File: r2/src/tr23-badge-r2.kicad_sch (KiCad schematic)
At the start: 60 parts, among them Q1 MMBT3904-TP, Q2 MMBT3904-TP, Q3 MMBT3904-TP, Y1 32.768kHz

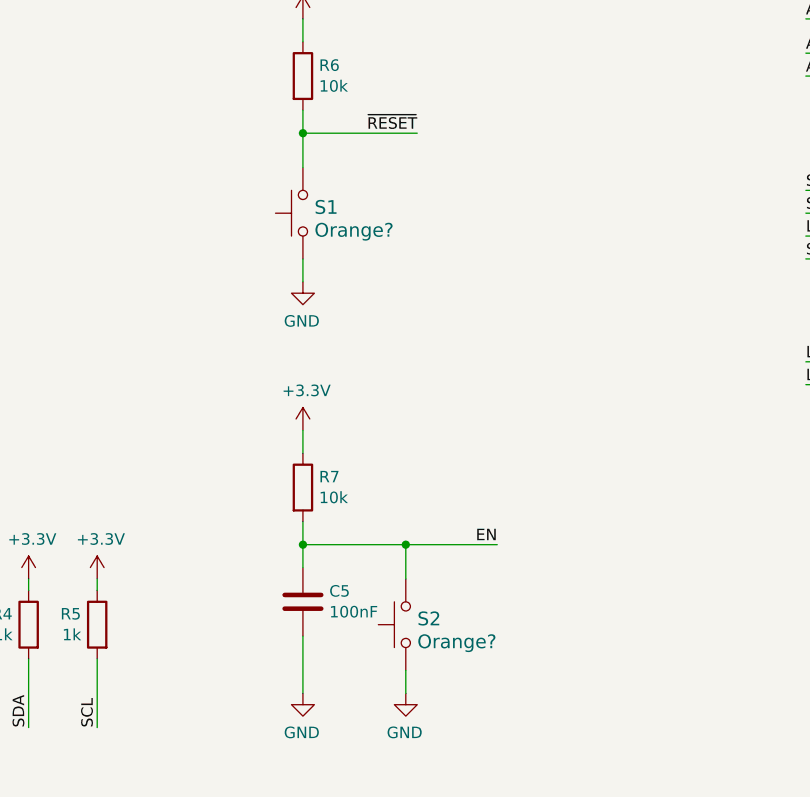
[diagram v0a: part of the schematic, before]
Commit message: Fix tactile switch symbols. By using a two-pin symbol rather than the truer 4-pin one, signals were shorted at the footprint
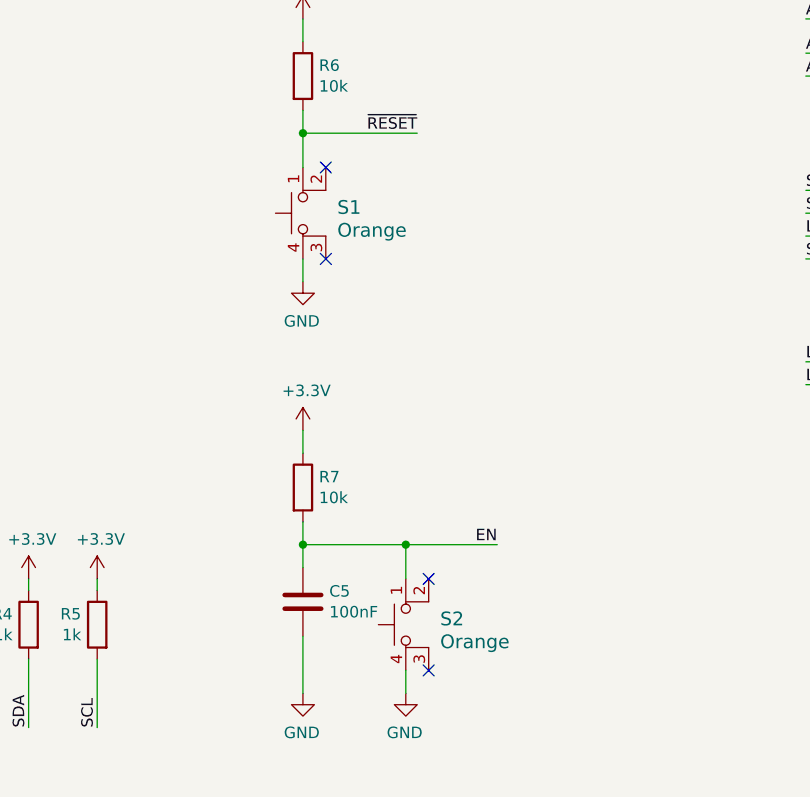
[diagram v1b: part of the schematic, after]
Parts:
- S1, S2: value Orange? -> Orange; symbol Switch:SW_Push -> Switch:SW_MEC_5E
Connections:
- net GND: now also S1.4 (A), S2.4 (A); no longer S1.2, S2.2
- no-connect marks 0 -> 4
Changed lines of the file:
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@@
   (junction (at 31.75 132.08) (diameter 0) (color 0 0 0 0)
   )
+  (no_connect (at 130.81 137.16))
+  (no_connect (at 142.24 172.72))
+  (no_connect (at 130.81 127))
+  (no_connect (at 142.24 182.88))
   (wire (pts (xy 195.58 129.54) (xy 184.15 129.54))
     (stroke (width 0) (type default))
@@
     )
   )
-  (symbol (lib_id "Switch:SW_Push") (at 128.27 132.08 90) (mirror x) (unit 1)
+  (symbol (lib_id "Switch:SW_MEC_5E") (at 130.81 132.08 90) (mirror x) (unit 1)
     (in_bom yes) (on_board yes) (dnp no) (fields_autoplaced)
-    (property "Reference" "S1" (at 129.54 131.445 90)
+    (property "Reference" "S1" (at 132.08 131.445 90)
       (effects (font (size 1.524 1.524)) (justify right))
     )
-    (property "Value" "Orange?" (at 129.54 133.985 90)
+    (property "Value" "Orange" (at 132.08 133.985 90)
       (effects (font (size 1.524 1.524)) (justify right))
     )
@@
       (effects (font (size 1.27 1.27)) hide)
     )
-    (property "Datasheet" "~" (at 123.19 132.08 0)
-      (effects (font (size 1.27 1.27)) hide)
-    )
-    (property "Digi-Key_PN" "CKN9112CT-ND" (at 118.11 137.16 0)
-      (effects (font (size 1.524 1.524)) (justify left) hide)
-    )
-    (property "MPN" "" (at 115.57 137.16 0)
-      (effects (font (size 1.524 1.524)) (justify left) hide)
-    )
-    (property "Category" "Switches" (at 113.03 137.16 0)
-      (effects (font (size 1.524 1.524)) (justify left) hide)
-    )
-    (property "Family" "Tactile Switches" (at 110.49 137.16 0)
-      (effects (font (size 1.524 1.524)) (justify left) hide)
-    )
-    (property "DK_Datasheet_Link" "https://www.ckswitches.com/media/1471/pts645.pdf" (at 107.95 137.16 0)
-      (effects (font (size 1.524 1.524)) (justify left) hide)
-    )
-    (property "DK_Detail_Page" "/product-detail/en/c-k/PTS645SM43SMTR92-LFS/CKN9112CT-ND/1146934" (at 105.41 137.16 0)
-      (effects (font (size 1.524 1.524)) (justify left) hide)
-    )
-    (property "Description" "SWITCH TACTILE SPST-NO 0.05A 12V" (at 102.87 137.16 0)
-      (effects (font (size 1.524 1.524)) (justify left) hide)
-    )
-    (property "Manufacturer" "C&K" (at 100.33 137.16 0)
-      (effects (font (size 1.524 1.524)) (justify left) hide)
-    )
-    (property "Status" "Active" (at 97.79 137.16 0)
+    (property "Datasheet" "http://www.apem.com/int/index.php?controller=attachment&id_attachment=1371" (at 123.19 132.08 0)
+      (effects (font (size 1.27 1.27)) hide)
+    )
+    (property "Digi-Key_PN" "CKN9112CT-ND" (at 120.65 137.16 0)
+      (effects (font (size 1.524 1.524)) (justify left) hide)
+    )
+    (property "MPN" "" (at 118.11 137.16 0)
+      (effects (font (size 1.524 1.524)) (justify left) hide)
+    )
+    (property "Category" "Switches" (at 115.57 137.16 0)
+      (effects (font (size 1.524 1.524)) (justify left) hide)
+    )
+    (property "Family" "Tactile Switches" (at 113.03 137.16 0)
+      (effects (font (size 1.524 1.524)) (justify left) hide)
+    )
+    (property "DK_Datasheet_Link" "https://www.ckswitches.com/media/1471/pts645.pdf" (at 110.49 137.16 0)
+      (effects (font (size 1.524 1.524)) (justify left) hide)
+    )
+    (property "DK_Detail_Page" "/product-detail/en/c-k/PTS645SM43SMTR92-LFS/CKN9112CT-ND/1146934" (at 107.95 137.16 0)
+      (effects (font (size 1.524 1.524)) (justify left) hide)
+    )
+    (property "Description" "SWITCH TACTILE SPST-NO 0.05A 12V" (at 105.41 137.16 0)
+      (effects (font (size 1.524 1.524)) (justify left) hide)
+    )
+    (property "Manufacturer" "C&K" (at 102.87 137.16 0)
+      (effects (font (size 1.524 1.524)) (justify left) hide)
+    )
+    (property "Status" "Active" (at 100.33 137.16 0)
       (effects (font (size 1.524 1.524)) (justify left) hide)
     )
     (pin "1")
     (pin "2")
+    (pin "3")
+    (pin "4")
     (instances
       (project "tr23-badge-r2"
@@
     )
   )
-  (symbol (lib_id "Switch:SW_Push") (at 139.7 177.8 90) (mirror x) (unit 1)
+  (symbol (lib_id "Switch:SW_MEC_5E") (at 142.24 177.8 90) (mirror x) (unit 1)
     (in_bom yes) (on_board yes) (dnp no) (fields_autoplaced)
-    (property "Reference" "S2" (at 140.97 177.165 90)
+    (property "Reference" "S2" (at 143.51 177.165 90)
       (effects (font (size 1.524 1.524)) (justify right))
     )
-    (property "Value" "Orange?" (at 140.97 179.705 90)
+    (property "Value" "Orange" (at 143.51 179.705 90)
       (effects (font (size 1.524 1.524)) (justify right))
     )
@@
       (effects (font (size 1.27 1.27)) hide)
     )
-    (property "Datasheet" "~" (at 134.62 177.8 0)
-      (effects (font (size 1.27 1.27)) hide)
-    )
-    (property "Digi-Key_PN" "CKN9112CT-ND" (at 129.54 182.88 0)
-      (effects (font (size 1.524 1.524)) (justify left) hide)
-    )
-    (property "MPN" "" (at 127 182.88 0)
-      (effects (font (size 1.524 1.524)) (justify left) hide)
-    )
-    (property "Category" "Switches" (at 124.46 182.88 0)
-      (effects (font (size 1.524 1.524)) (justify left) hide)
-    )
-    (property "Family" "Tactile Switches" (at 121.92 182.88 0)
-      (effects (font (size 1.524 1.524)) (justify left) hide)
-    )
-    (property "DK_Datasheet_Link" "https://www.ckswitches.com/media/1471/pts645.pdf" (at 119.38 182.88 0)
-      (effects (font (size 1.524 1.524)) (justify left) hide)
-    )
-    (property "DK_Detail_Page" "/product-detail/en/c-k/PTS645SM43SMTR92-LFS/CKN9112CT-ND/1146934" (at 116.84 182.88 0)
-      (effects (font (size 1.524 1.524)) (justify left) hide)
-    )
-    (property "Description" "SWITCH TACTILE SPST-NO 0.05A 12V" (at 114.3 182.88 0)
-      (effects (font (size 1.524 1.524)) (justify left) hide)
-    )
-    (property "Manufacturer" "C&K" (at 111.76 182.88 0)
-      (effects (font (size 1.524 1.524)) (justify left) hide)
-    )
-    (property "Status" "Active" (at 109.22 182.88 0)
+    (property "Datasheet" "http://www.apem.com/int/index.php?controller=attachment&id_attachment=1371" (at 134.62 177.8 0)
+      (effects (font (size 1.27 1.27)) hide)
+    )
+    (property "Digi-Key_PN" "CKN9112CT-ND" (at 132.08 182.88 0)
+      (effects (font (size 1.524 1.524)) (justify left) hide)
+    )
+    (property "MPN" "" (at 129.54 182.88 0)
+      (effects (font (size 1.524 1.524)) (justify left) hide)
+    )
+    (property "Category" "Switches" (at 127 182.88 0)
+      (effects (font (size 1.524 1.524)) (justify left) hide)
+    )
+    (property "Family" "Tactile Switches" (at 124.46 182.88 0)
+      (effects (font (size 1.524 1.524)) (justify left) hide)
+    )
+    (property "DK_Datasheet_Link" "https://www.ckswitches.com/media/1471/pts645.pdf" (at 121.92 182.88 0)
+      (effects (font (size 1.524 1.524)) (justify left) hide)
+    )
+    (property "DK_Detail_Page" "/product-detail/en/c-k/PTS645SM43SMTR92-LFS/CKN9112CT-ND/1146934" (at 119.38 182.88 0)
+      (effects (font (size 1.524 1.524)) (justify left) hide)
+    )
+    (property "Description" "SWITCH TACTILE SPST-NO 0.05A 12V" (at 116.84 182.88 0)
+      (effects (font (size 1.524 1.524)) (justify left) hide)
+    )
+    (property "Manufacturer" "C&K" (at 114.3 182.88 0)
+      (effects (font (size 1.524 1.524)) (justify left) hide)
+    )
+    (property "Status" "Active" (at 111.76 182.88 0)
       (effects (font (size 1.524 1.524)) (justify left) hide)
     )
     (pin "1")
     (pin "2")
-    (instances
-      (project "tr23-badge-r2"
+    (pin "3")
+    (pin "4")
+    (instances
+      (project "tr23-badge-r2"

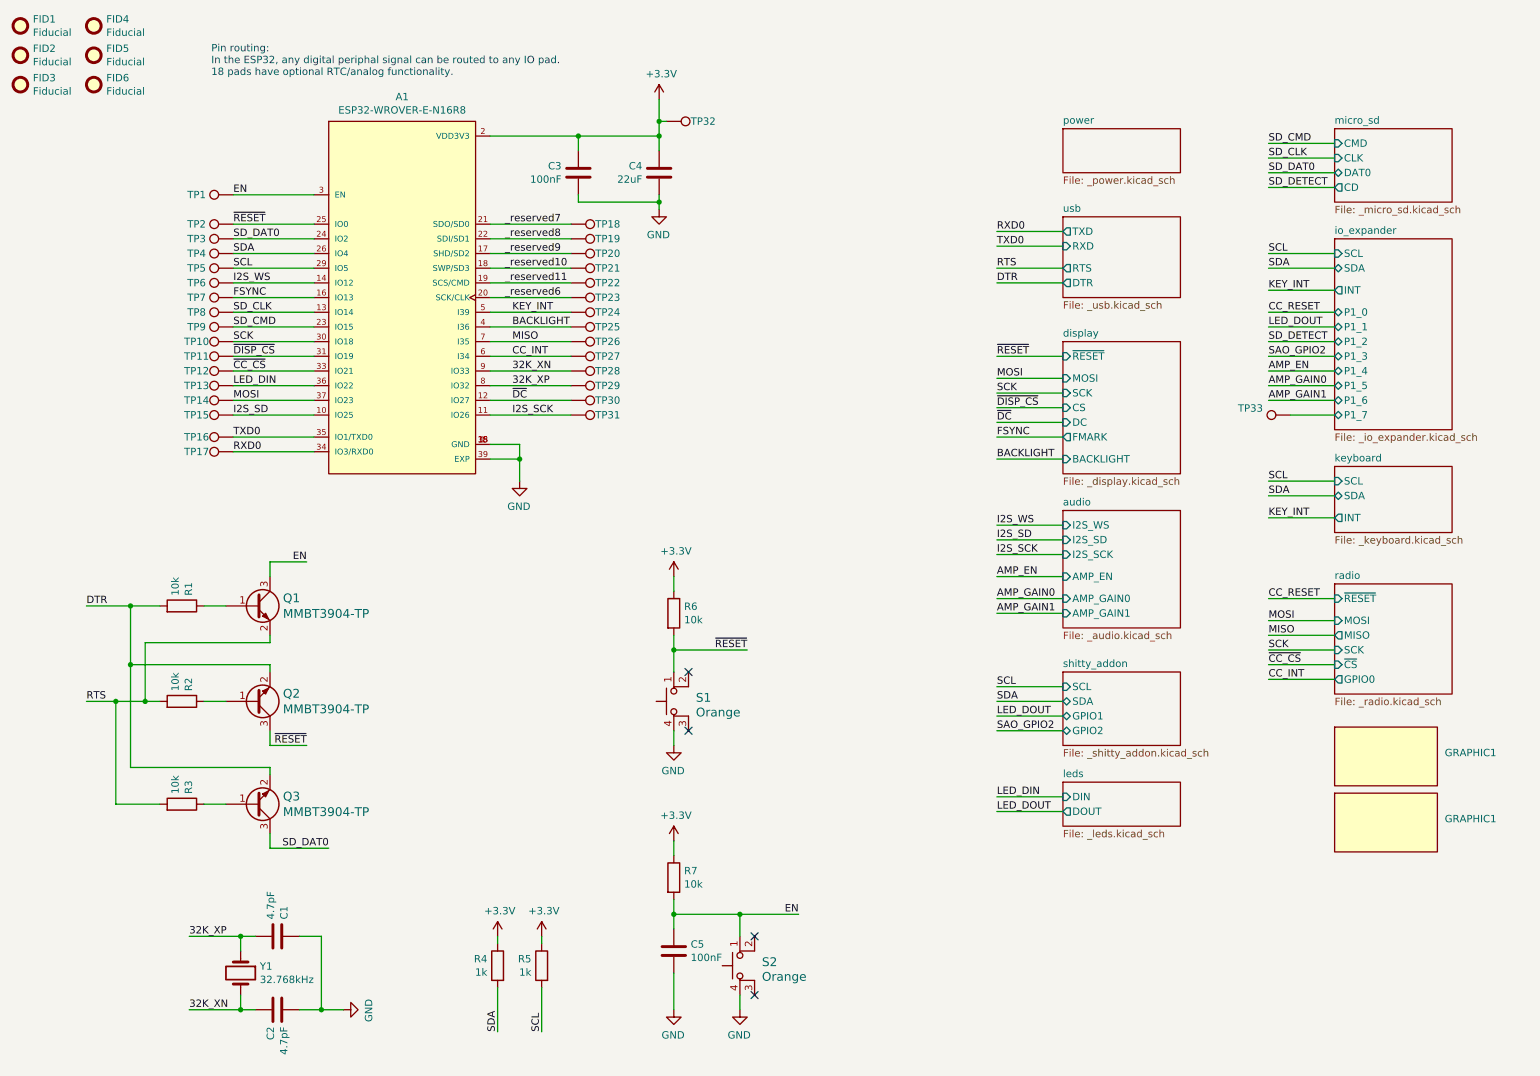
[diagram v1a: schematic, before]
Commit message: Switch around some signals on the ESP32 so: 1) BACKLIGHT is not on an input-only pin 2) The IO0 bootloader line is shared with the radio CS line rather than    the display reset line, so display doesn't get cleared when you press    the button
Also, updating Kicad bumps some version signifier in the files, so there
is some file noise.
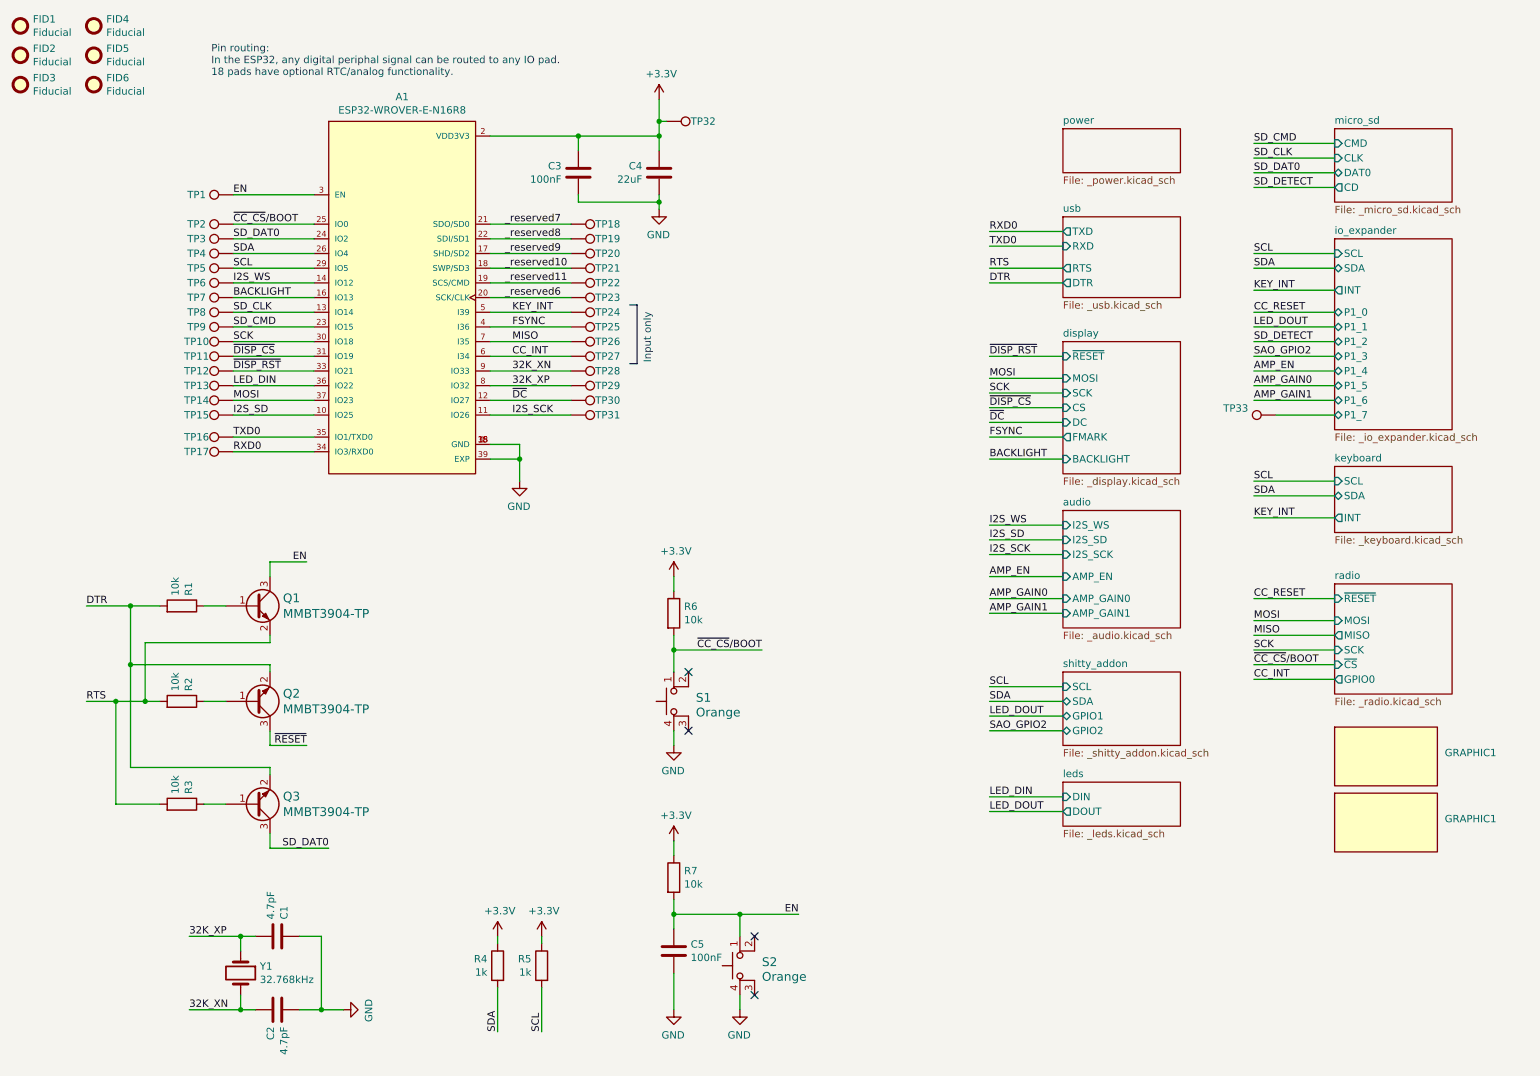
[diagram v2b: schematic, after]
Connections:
- net BACKLIGHT: now also A1.16 (IO13), TP7.1; no longer A1.4 (I36), TP25.1
- net FSYNC: now also A1.4 (I36), TP25.1; no longer A1.16 (IO13), TP7.1
- net ~{RESET}: no longer A1.25 (IO0), R6.2, S1.1, TP2.1
- net ~{CC_CS} renamed ~{DISP_RST}
- new net ~{CC_CS}/BOOT: A1.25 (IO0), R6.2, S1.1, TP2.1
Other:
- note added: "Input only"
- moved on the sheet: TP33

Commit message: Fix off-grid ERC errors so whole schematic is on 1.27mm grid
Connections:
- net ~{RESET} is gone; now on net ~{CC_CS}/BOOT0: Q2.3 (C)
- net SD_DAT0 renamed SD_DAT0/BOOT2
- net ~{CC_CS}/BOOT renamed ~{CC_CS}/BOOT0
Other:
- moved on the sheet: TP1, TP10, TP11, TP12, TP13, TP14, TP15, TP16, TP17, TP2, TP3, TP33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

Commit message: Update WROVER with renamed footprint
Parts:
- A1: footprint jeffmakes-footprints:ESP32-WROVER-I -> jeffmakes-footprints:ESP32-WROVER
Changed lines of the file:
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@@
       (effects (font (size 1.27 1.27)))
     )
-    (property "Footprint" "jeffmakes-footprints:ESP32-WROVER-I" (at 81.28 62.23 0)
+    (property "Footprint" "jeffmakes-footprints:ESP32-WROVER" (at 81.28 62.23 0)
       (effects (font (size 1.27 1.27)) (justify left bottom) hide)
     )

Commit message: Update WROVER with symbol including NC pins.
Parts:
- A1: symbol j_RF_Module:ESP32-WROVER-I -> j_RF_Module:ESP32-WROVER; Manufacturer Espressif -> Espressif Systems
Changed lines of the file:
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@@
     (effects (font (size 1.27 1.27)) (justify left bottom))
   )
-  (symbol (lib_id "j_RF_Module:ESP32-WROVER-I") (at 81.28 62.23 0) (unit 1)
+  (symbol (lib_id "j_RF_Module:ESP32-WROVER") (at 81.28 62.23 0) (unit 1)
     (in_bom yes) (on_board yes) (dnp no)
     (property "Reference" "A1" (at 81.28 27.5082 0)
@@
       (effects (font (size 1.27 1.27)) (justify left bottom) hide)
     )
-    (property "Datasheet" "Module Espressif Systems" (at 81.28 62.23 0)
+    (property "Datasheet" "Espressif Systems" (at 81.28 62.23 0)
       (effects (font (size 1.27 1.27)) (justify left bottom) hide)
     )
@@
       (effects (font (size 1.27 1.27)) (justify left bottom) hide)
     )
-    (property "Manufacturer" "Espressif" (at 81.28 62.23 0)
+    (property "Manufacturer" "Espressif Systems" (at 81.28 62.23 0)
       (effects (font (size 1.27 1.27)) (justify left bottom) hide)
     )
@@
     (pin "8")
     (pin "9")
+    (pin "27")
+    (pin "28")
+    (pin "32")
     (instances
       (project "tr23-badge-r2"
